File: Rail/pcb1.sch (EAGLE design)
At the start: 45 parts, among them J6 638207222005, J7 638207222005, U4 TLE9250VSJ, X1 S4P-VH

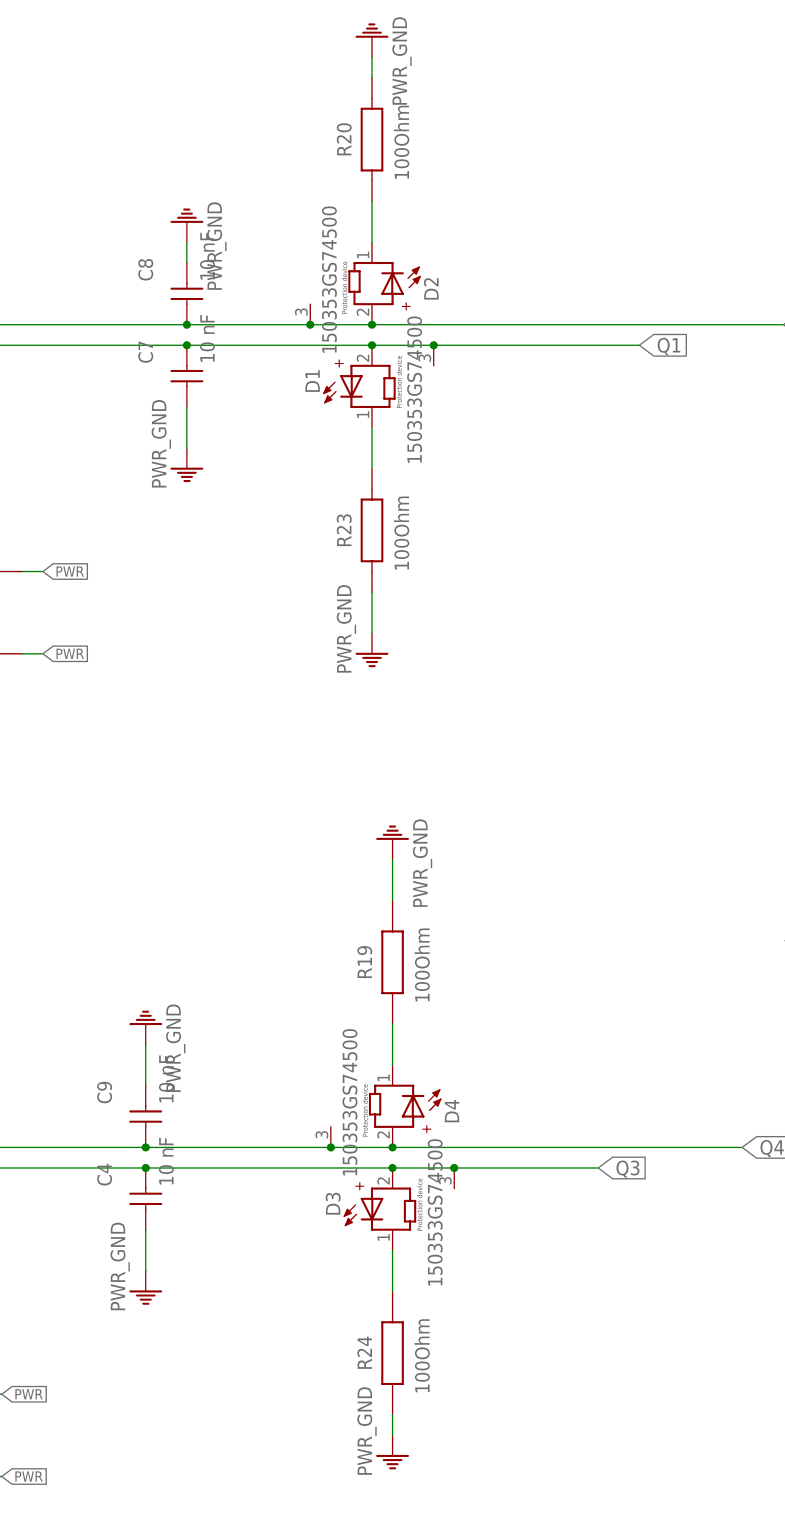
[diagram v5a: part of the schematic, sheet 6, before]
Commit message: smaller LED
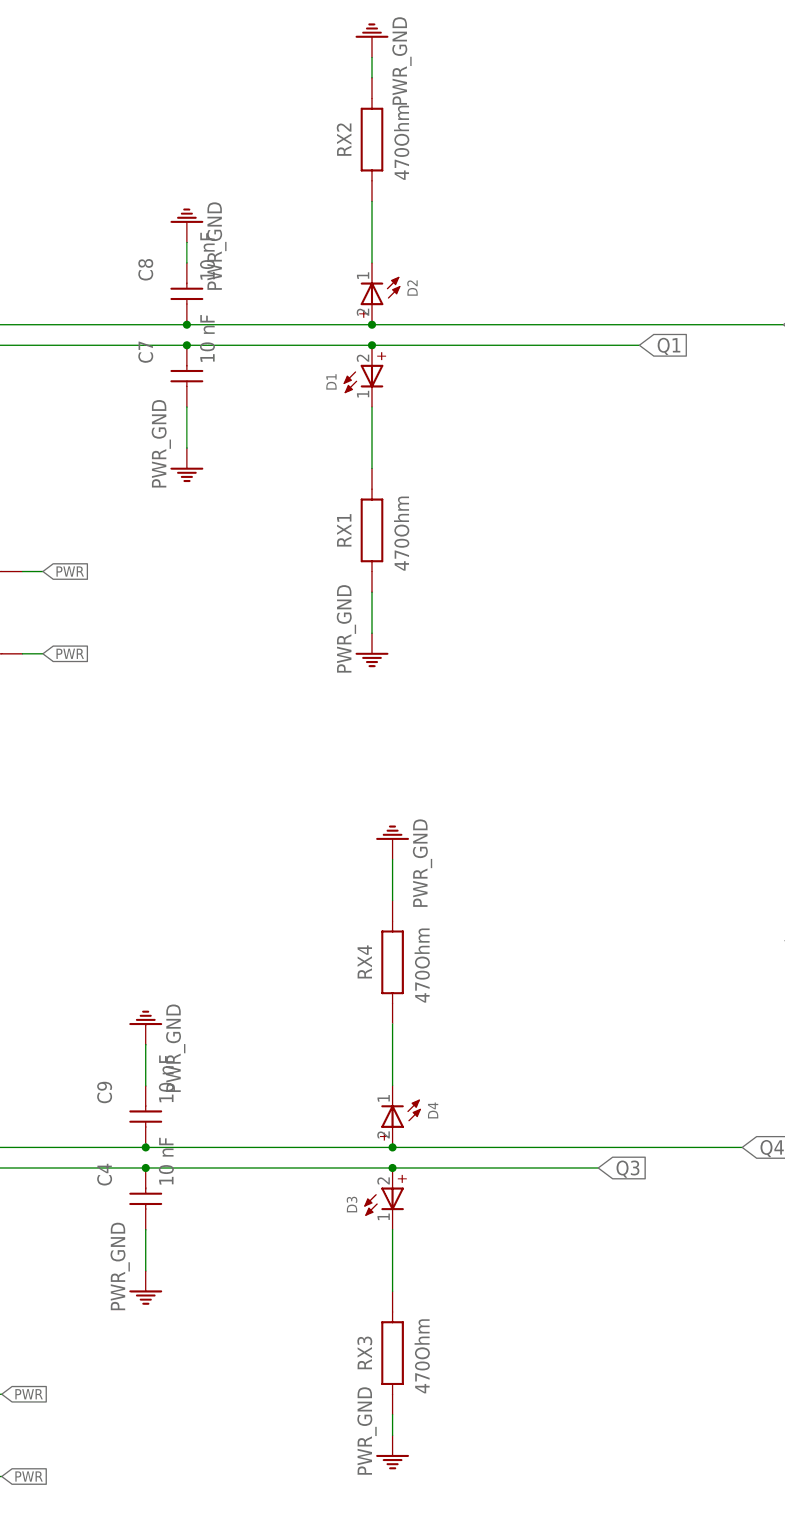
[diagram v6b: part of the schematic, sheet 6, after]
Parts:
- removed R19, R20, R23, R24: 100Ohm, Wurth_Resistor_WRIS-KWKB:WRIS-KWKB_0612_561020132008
- added RX1, RX2, RX3, RX4: 470Ohm, Wurth_Resistor_WRIS-KWKB:WRIS-KWKB_0612_561020132023
- D1, D2, D3, D4: value 150353GS74500 -> (none); device LED:WL-SMDC_3535_150353GS74500 -> Wurth_LEDs_WL-SMRW:WL-SMRW_1206_DOME_156120VS82500_NOR
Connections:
- net N$1: now also RX4.1; no longer R19.1
- net N$6: now also RX2.1; no longer R20.1
- net N$8: now also RX1.2; no longer R23.2
- net N$9: now also RX3.2; no longer R24.2
- net PWR_GND: now also RX1.1, RX2.2, RX3.1, RX4.2; no longer R19.2, R20.2, R23.1, R24.1
- net Q1: no longer D1.COOL
- net Q2: no longer D2.COOL
- net Q3: no longer D3.COOL
- net Q4: no longer D4.COOL

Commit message: LED and Resisotr !
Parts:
- RX1, RX2, RX3, RX4: value 470Ohm -> 510mOhm; device Wurth_Resistor_WRIS-KWKB:WRIS-KWKB_0612_561020132023 -> Wurth_Resistor_WRIS-KWKH:WRIS-KWKH_0612_561070332078
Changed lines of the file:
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@@
 <part name="C12" library="Wurth_Capacitors_WCAP-CSGP" library_urn="urn:adsk.eagle:library:18488985" deviceset="WCAP-CSGP_0805_H1.25" device="_10V(DC)" package3d_urn="urn:adsk.eagle:package:18489127/2" technology="_885012107011" value="22  µF "/>
 <part name="D0" library="Wurth_EMC Components_WE-TVSP" library_urn="urn:adsk.eagle:library:14283044" deviceset="WE-TVSP_DO-214AB_3000W_BI" device="" package3d_urn="urn:adsk.eagle:package:12146529/2" technology="_824551331" value="33V"/>
-<part name="RX4" library="Wurth_Resistor_WRIS-KWKB" library_urn="urn:adsk.eagle:library:13351500" deviceset="WRIS-KWKB_0612" device="" package3d_urn="urn:adsk.eagle:package:13351506/2" technology="_561020132023" value="470Ohm"/>
-<part name="RX2" library="Wurth_Resistor_WRIS-KWKB" library_urn="urn:adsk.eagle:library:13351500" deviceset="WRIS-KWKB_0612" device="" package3d_urn="urn:adsk.eagle:package:13351506/2" technology="_561020132023" value="470Ohm"/>
-<part name="RX1" library="Wurth_Resistor_WRIS-KWKB" library_urn="urn:adsk.eagle:library:13351500" deviceset="WRIS-KWKB_0612" device="" package3d_urn="urn:adsk.eagle:package:13351506/2" technology="_561020132023" value="470Ohm"/>
-<part name="RX3" library="Wurth_Resistor_WRIS-KWKB" library_urn="urn:adsk.eagle:library:13351500" deviceset="WRIS-KWKB_0612" device="" package3d_urn="urn:adsk.eagle:package:13351506/2" technology="_561020132023" value="470Ohm"/>
+<part name="RX4" library="Wurth_Resistor_WRIS-KWKH" library_urn="urn:adsk.eagle:library:13353576" deviceset="WRIS-KWKH_0612" device="" package3d_urn="urn:adsk.eagle:package:13353581/2" technology="_561070332078" value="510mOhm"/>
+<part name="RX2" library="Wurth_Resistor_WRIS-KWKH" library_urn="urn:adsk.eagle:library:13353576" deviceset="WRIS-KWKH_0612" device="" package3d_urn="urn:adsk.eagle:package:13353581/2" technology="_561070332078" value="510mOhm"/>
+<part name="RX1" library="Wurth_Resistor_WRIS-KWKH" library_urn="urn:adsk.eagle:library:13353576" deviceset="WRIS-KWKH_0612" device="" package3d_urn="urn:adsk.eagle:package:13353581/2" technology="_561070332078" value="510mOhm"/>
+<part name="RX3" library="Wurth_Resistor_WRIS-KWKH" library_urn="urn:adsk.eagle:library:13353576" deviceset="WRIS-KWKH_0612" device="" package3d_urn="urn:adsk.eagle:package:13353581/2" technology="_561070332078" value="510mOhm"/>
 <part name="D5" library="Wurth_EMC Components_WE-TVSP" library_urn="urn:adsk.eagle:library:14283044" deviceset="WE-TVSP_DO-214AB_3000W_BI" device="" package3d_urn="urn:adsk.eagle:package:12146529/2" technology="_824551331" value="33V"/>
 <part name="R1" library="resistor" library_urn="urn:adsk.eagle:library:348" deviceset="R-EU_" device="R0805" package3d_urn="urn:adsk.eagle:package:23553/2" value="60R"/>
